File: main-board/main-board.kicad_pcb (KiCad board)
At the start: 2 copper layers, 210 x 130 mm, 172 parts, among them J1 PWR_SELECT, J10 Conn_02x05_Odd_Even, J11 Conn_02x05_Odd_Even, J12 Conn_02x05_Odd_Even, J13 Conn_02x05_Odd_Even, J14 Conn_02x05_Odd_Even, J15 Conn_02x05_Odd_Even, J16 COMM_3, J17 Modular board connector, J18 PWR_EXT_1, J19 PWR_EXT_2, J2 COMM1, J20 COMM_4, J21 COMM_OUT, J3 ICSP, J4 Conn_02x03_Top_Bottom, J5 COMM_2, J7 Conn_02x05_Odd_Even, J8 Conn_02x05_Odd_Even, J9 Conn_02x05_Odd_Even, SW1 RESET, SW10 SW_Push, SW11 SW_Push, SW12 SW_SP3T_x08, SW13 SW_Push, SW14 SW_Push, SW15 SW_Push, SW16 SW_Push, SW17 SW_Push, SW18 SW_Push, SW19 SW_Push, SW2 BTN_LEVEL, SW20 SW_Push, SW21 SW_SP3T_x08, SW22 SW_Push, SW23 SW_Push, SW24 SW_Push, SW25 SW_Push, SW26 SW_Push, SW27 SW_Push, SW28 SW_Push, SW29 SW_Push, SW3 LED_GND, SW30 SW_SP3T_x08, SW31 SW_Push, SW32 SW_Push, SW33 SW_Push, SW34 SW_Push, SW35 SW_Push, SW36 SW_Push, SW37 SW_Push, SW38 SW_Push, SW39 SW_SP3T_x08, SW4 SW_Push, SW41 PWR_EN, SW5 SW_Push, SW6 SW_Push, SW7 SW_Push, SW8 SW_Push, SW9 SW_Push, U1 LM2576HVS-5, U2 AP1117-33, U3 AP1117-18, U4 FT232RL

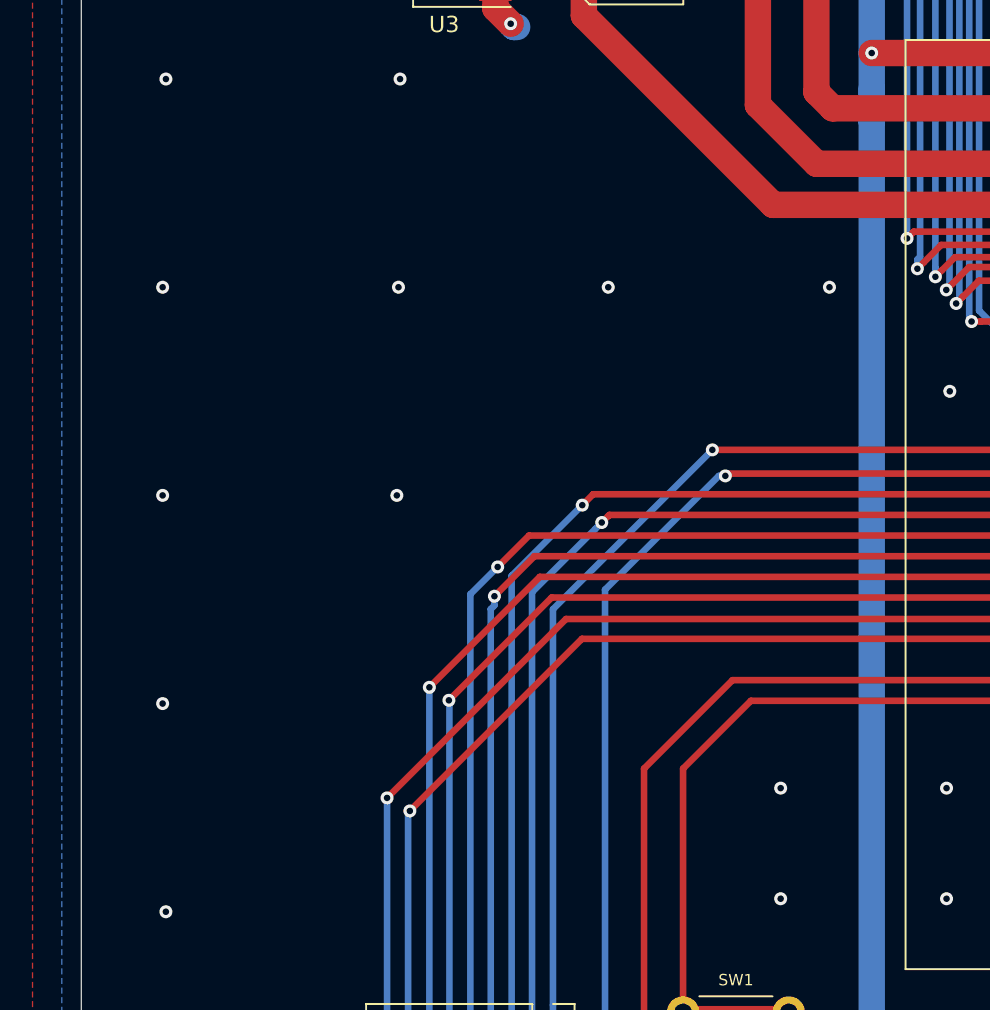
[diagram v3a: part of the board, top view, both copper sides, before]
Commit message: Added module board hole
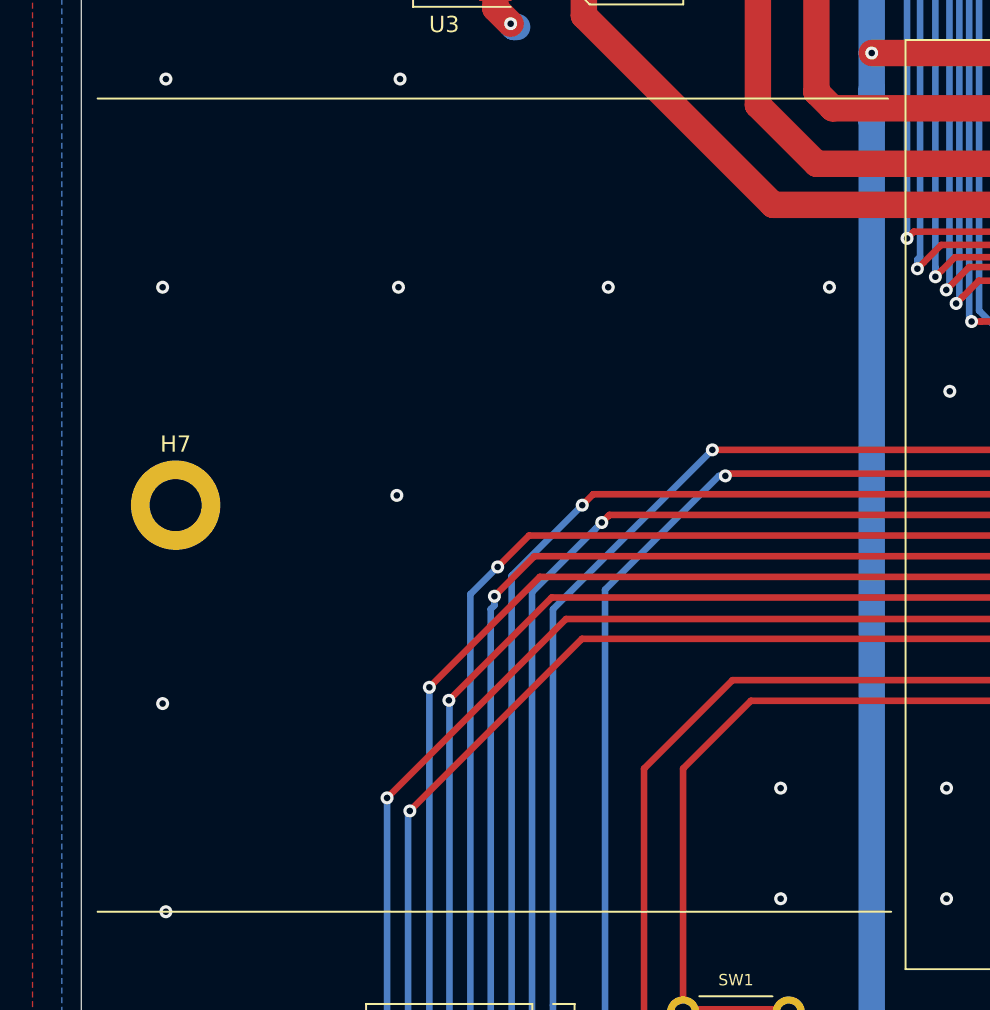
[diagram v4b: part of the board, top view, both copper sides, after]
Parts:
- added H7: MountingHole_Pad, MountingHole:MountingHole_3.2mm_M3_ISO14580_Pad, F.Cu at (42.8, 108.8)
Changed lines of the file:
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@@
   (general
     (thickness 1.6)
-    (drawings 78)
+    (drawings 83)
     (tracks 2027)
     (zones 0)
-    (modules 172)
+    (modules 173)
     (nets 137)
   )
   (page A4)
   (layers
-    (0 F.Cu signal)
-    (31 B.Cu signal)
+    (0 F.Cu signal hide)
+    (31 B.Cu signal hide)
     (32 B.Adhes user hide)
     (33 F.Adhes user hide)
@@
     (38 B.Mask user hide)
     (39 F.Mask user)
-    (40 Dwgs.User user hide)
+    (40 Dwgs.User user)
     (41 Cmts.User user hide)
     (42 Eco1.User user hide)
     (43 Eco2.User user hide)
     (44 Edge.Cuts user)
-    (45 Margin user hide)
+    (45 Margin user)
     (46 B.CrtYd user hide)
     (47 F.CrtYd user hide)
@@
     (add_net "Net-(J17-Pad30)")
     (add_net "Net-(J17-Pad32)")
+    (add_net "Net-(J17-Pad34)")
+    (add_net "Net-(J17-Pad56)")
     (add_net "Net-(J17-Pad58)")
     (add_net "Net-(J17-Pad60)")
+    (add_net "Net-(J17-Pad75)")
     (add_net "Net-(J21-Pad2)")
     (add_net "Net-(J21-Pad3)")
@@
     (add_net "Net-(R7-Pad1)")
     (add_net "Net-(R7-Pad2)")
+    (add_net "Net-(SW41-Pad3)")
+    (add_net "Net-(U4-Pad10)")
+    (add_net "Net-(U4-Pad12)")
+    (add_net "Net-(U4-Pad13)")
+    (add_net "Net-(U4-Pad14)")
     (add_net "Net-(U4-Pad15)")
     (add_net "Net-(U4-Pad16)")
+    (add_net "Net-(U4-Pad19)")
+    (add_net "Net-(U4-Pad27)")
+    (add_net "Net-(U4-Pad28)")
+    (add_net "Net-(U4-Pad4)")
+    (add_net "Net-(U4-Pad6)")
+    (add_net "Net-(U4-Pad9)")
     (add_net VBUS)
   )
@@
     (uvia_drill 0.1)
   )
+  (module MountingHole:MountingHole_3.2mm_M3_ISO14580_Pad (layer F.Cu)
+    (at 42.8 108.8)
+    (descr "Mounting Hole 3.2mm, M3, ISO14580")
+    (tags "mounting hole 3.2mm m3 iso14580")
+    (attr virtual)
+    (fp_text reference H7 (at 0 -3.75) (layer F.SilkS)
+      (effects (font (size 1 1) (thickness 0.15)))
+    )
+    (fp_text value MountingHole_Pad (at 0 3.75) (layer F.Fab)
+      (effects (font (size 1 1) (thickness 0.15)))
+    )
+    (fp_circle (center 0 0) (end 3 0) (layer F.CrtYd) (width 0.05))
+    (fp_circle (center 0 0) (end 2.75 0) (layer Cmts.User) (width 0.15))
+    (fp_text user %R (at 0.3 0) (layer F.Fab)
+      (effects (font (size 1 1) (thickness 0.15)))
+    )
+    (pad 1 thru_hole circle (at 0 0) (size 5.5 5.5) (drill 3.2) (layers *.Cu *.Mask)
+      (net 1 GND))
+  )
   (module Connector_PinHeader_2.54mm:PinHeader_2x03_P2.54mm_Vertical (layer F.Cu)
     (at 154 124.4 270)
@@
     )
   )
+  (dimension 25 (width 0.15) (layer Dwgs.User)
+    (gr_text "25,000 mm" (at 29.9 96.3 270) (layer Dwgs.User)
+      (effects (font (size 1 1) (thickness 0.15)))
+    )
+    (feature1 (pts (xy 38 108.8) (xy 30.613579 108.8)))
+    (feature2 (pts (xy 38 83.8) (xy 30.613579 83.8)))
+    (crossbar (pts (xy 31.2 83.8) (xy 31.2 108.8)))
+    (arrow1a (pts (xy 31.2 108.8) (xy 30.613579 107.673496)))
+    (arrow1b (pts (xy 31.2 108.8) (xy 31.786421 107.673496)))
+    (arrow2a (pts (xy 31.2 83.8) (xy 30.613579 84.926504)))
+    (arrow2b (pts (xy 31.2 83.8) (xy 31.786421 84.926504)))
+  )
+  (dimension 50 (width 0.15) (layer Dwgs.User)
+    (gr_text "50,000 mm" (at 20.9 108.8 270) (layer Dwgs.User)
+      (effects (font (size 1 1) (thickness 0.15)))
+    )
+    (feature1 (pts (xy 38 133.8) (xy 21.613579 133.8)))
+    (feature2 (pts (xy 38 83.8) (xy 21.613579 83.8)))
+    (crossbar (pts (xy 22.2 83.8) (xy 22.2 133.8)))
+    (arrow1a (pts (xy 22.2 133.8) (xy 21.613579 132.673496)))
+    (arrow1b (pts (xy 22.2 133.8) (xy 22.786421 132.673496)))
+    (arrow2a (pts (xy 22.2 83.8) (xy 21.613579 84.926504)))
+    (arrow2b (pts (xy 22.2 83.8) (xy 22.786421 84.926504)))
+  )
+  (gr_line (start 84.4 108.8) (end 47 108.8) (layer Dwgs.User) (width 0.15))
+  (gr_line (start 86.8 133.8) (end 38 133.8) (layer F.SilkS) (width 0.12))
+  (gr_line (start 86.6 83.8) (end 38 83.8) (layer F.SilkS) (width 0.12))
+  (dimension 45 (width 0.12) (layer Dwgs.User)
+    (gr_text "45,000 mm" (at 65.3 121.47) (layer Dwgs.User)
+      (effects (font (size 1 1) (thickness 0.15)))
+    )
+    (feature1 (pts (xy 42.8 107.8) (xy 42.8 120.786421)))
+    (feature2 (pts (xy 87.8 107.8) (xy 87.8 120.786421)))
+    (crossbar (pts (xy 87.8 120.2) (xy 42.8 120.2)))
+    (arrow1a (pts (xy 42.8 120.2) (xy 43.926504 119.613579)))
+    (arrow1b (pts (xy 42.8 120.2) (xy 43.926504 120.786421)))
+    (arrow2a (pts (xy 87.8 120.2) (xy 86.673496 119.613579)))
+    (arrow2b (pts (xy 87.8 120.2) (xy 86.673496 120.786421)))
+  )
   (gr_line (start 95.932 57.52) (end 95.932 56.4) (layer F.SilkS) (width 0.4))
   (gr_line (start 98.472 57.52) (end 98.472 56.4) (layer F.SilkS) (width 0.4))
@@
     (arrow2b (pts (xy 51.2 155.8) (xy 52.326504 155.213579)))
   )
-  (dimension 53 (width 0.15) (layer Dwgs.User)
-    (gr_text "53,000 mm" (at 24.7 107.5 270) (layer Dwgs.User)
-      (effects (font (size 1 1) (thickness 0.15)))
-    )
-    (feature1 (pts (xy 87 134) (xy 25.413579 134)))
-    (feature2 (pts (xy 87 81) (xy 25.413579 81)))
-    (crossbar (pts (xy 26 81) (xy 26 134)))
-    (arrow1a (pts (xy 26 134) (xy 25.413579 132.873496)))
-    (arrow1b (pts (xy 26 134) (xy 26.586421 132.873496)))
-    (arrow2a (pts (xy 26 81) (xy 25.413579 82.126504)))
-    (arrow2b (pts (xy 26 81) (xy 26.586421 82.126504)))
-  )
   (dimension 130 (width 0.15) (layer Dwgs.User)

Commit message: Updates
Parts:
- added [BRD_REF]: LOGO_BRD_REF, qboards_aesthetics:logo_url-10mm, F.Cu at (193.4, 138.6)
- added [BRD_REF]: LOGO_BRD_REF, qboards_aesthetics:logo_url-20mm, F.Cu at (62.0, 108.8)
- moved R8 7.60 mm to (136.0, 124.6)
- moved R9 7.60 mm to (136.0, 126.8)
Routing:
- net GND: track 129.5 -> 115.9 mm
- net Net-(J4-Pad2): track 12.2 -> 18.9 mm
- net VBUS: track 886.8 -> 892.5 mm
- net Net-(J4-Pad1): track 13.5 -> 19.0 mm
- net /PORT_D_BTN_LEVEL: track 162.3 -> 161.2 mm
- net /PORT_C_BTN_LEVEL: track 202.2 -> 203.0 mm

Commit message: Updated footprints
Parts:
- removed [BRD_REF]: LOGO_BRD_REF, qboards_aesthetics:logo_url-10mm
- removed [BRD_REF]: LOGO_BRD_REF, qboards_aesthetics:logo_url-20mm
- C1, C2, C3, C4: footprint Capacitor_SMD:CP_Elec_6.3x5.7 -> Capacitor_SMD:CP_Elec_8x10.5
- D5: footprint Diode_SMD:D_0805_2012Metric_Pad1.15x1.40mm_HandSolder -> Diode_SMD:D_SOD-323_HandSoldering
- L1: footprint Inductor_SMD:L_1812_4532Metric_Pad1.30x3.40mm_HandSolder -> Inductor_SMD:L_6.3x6.3_H3
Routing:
- net Net-(C2-Pad1): track 39.6 -> 41.4 mm
- net Net-(J1-Pad3): track 19.6 -> 20.3 mm

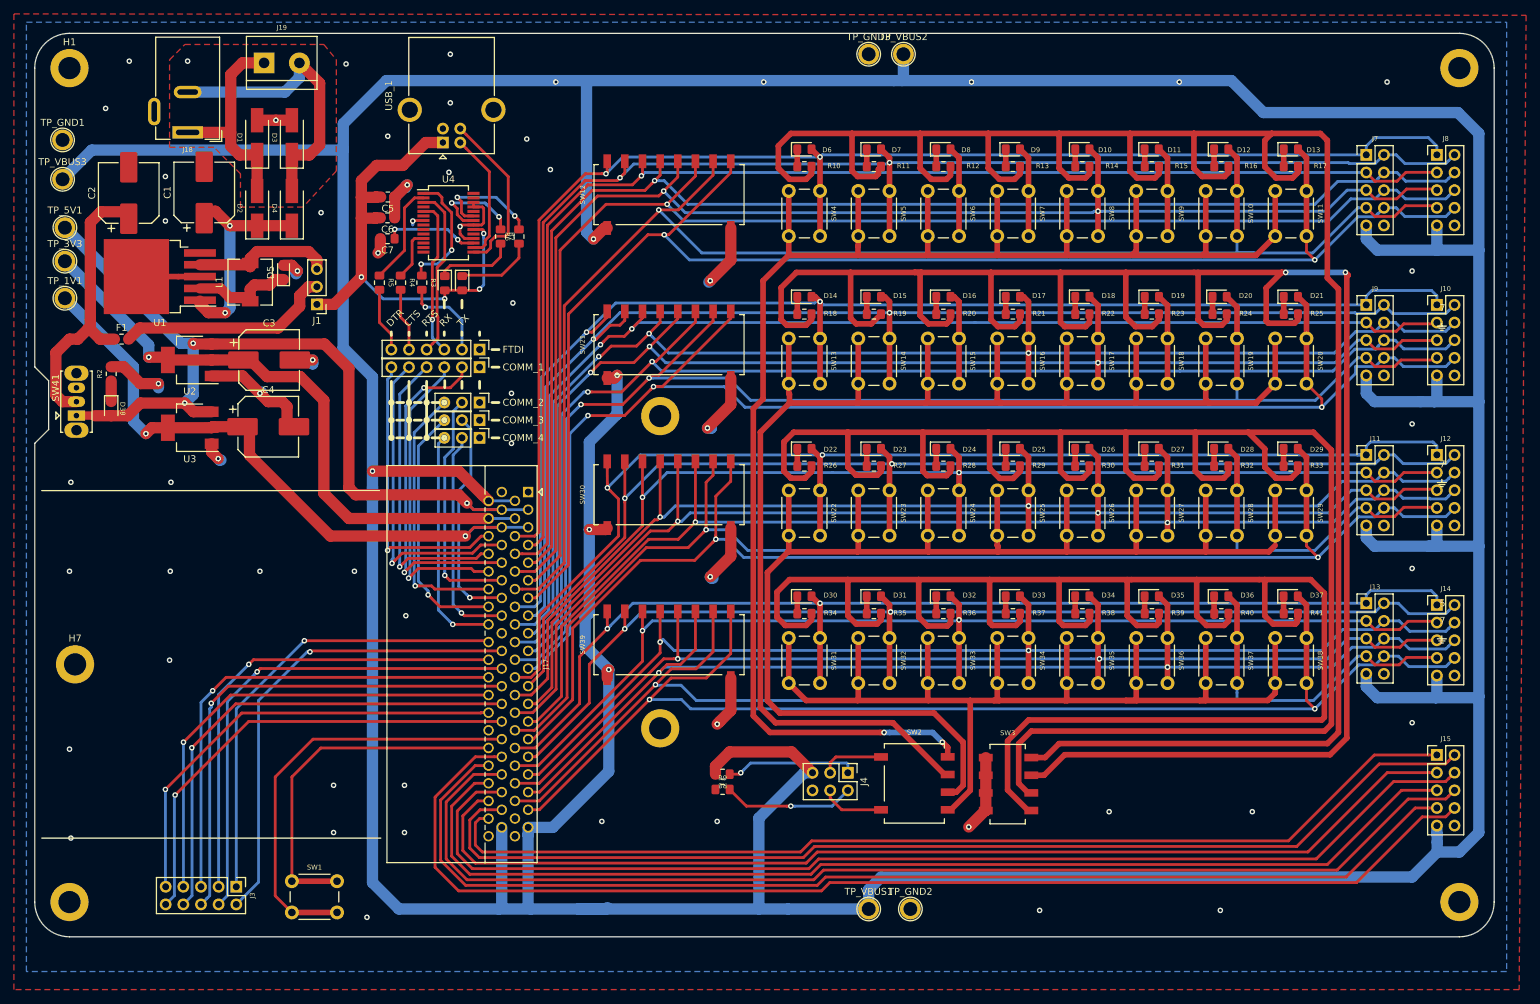
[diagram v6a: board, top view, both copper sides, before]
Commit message: Updated silkscreens
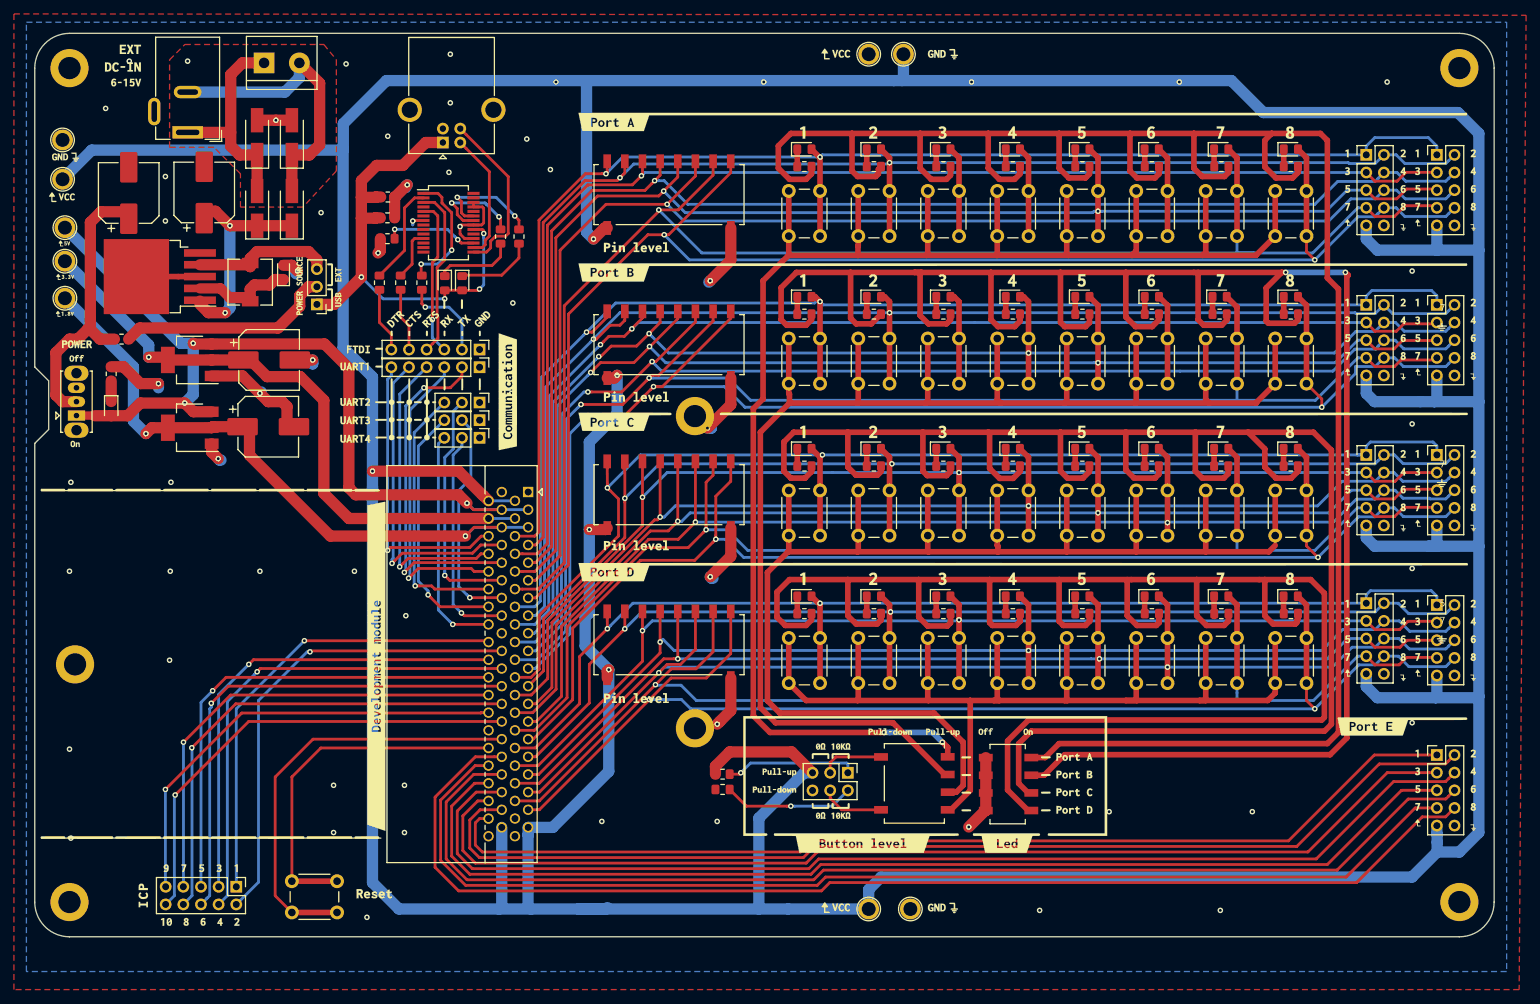
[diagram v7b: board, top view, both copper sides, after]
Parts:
- added ?: , , F.Cu at (90.9, 71.1)
- moved H5 5.00 mm to (132.0, 73.1)
- moved H6 5.00 mm to (132.0, 118.0)
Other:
- board text added: "0\U+03A9"
- board text added: "1"
- board text added: "1.8V"
- board text added: "10"
- board text added: "10K\U+03A9"
- board text added: "2"
- board text added: "3"
- board text added: "3.3V"
- board text added: "4"
- board text added: "5V"
- board text added: "6"
- board text added: "6-15V"
- board text added: "8"
- board text added: "9"
- board text added: "Button level"
- board text added: "Communication"
- board text added: "DC-IN"
- board text added: "Development module"
- board text added: "EXT"
- board text added: "GND"
- board text added: "ICP"
- board text added: "Led"
- board text added: "Off"
- board text added: "On"
- board text added: "POWER"
- board text added: "POWER SOURCE"
- board text added: "Pin level"
- board text added: "Port A"
- board text added: "Port B"
- board text added: "Port C"
- board text added: "Port D"
- board text added: "Port E"
- board text added: "Pull-down"
- board text added: "Pull-up"
- board text added: "Reset"
- board text added: "UART1"
- board text added: "UART2"
- board text added: "UART3"
- board text added: "UART4"
- board text added: "USB"
- board text added: "VCC"
- board text removed: "COMM_1"
- board text removed: "COMM_2"
- board text removed: "COMM_3"
- board text removed: "COMM_4"

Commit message: Cleaned up Dwgs.User
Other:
- board text removed: "0\U+03A9"
- board text removed: "1"
- board text removed: "1.8V"
- board text removed: "10"
- board text removed: "10K\U+03A9"
- board text removed: "2"
- board text removed: "3"
- board text removed: "3.3V"
- board text removed: "4"
- board text removed: "5V"
- board text removed: "6"
- board text removed: "6-15V"
- board text removed: "8"
- board text removed: "9"
- board text removed: "Button level"
- board text removed: "CTS"
- board text removed: "Communication"
- board text removed: "DC-IN"
- board text removed: "DTR"
- board text removed: "Development module"
- board text removed: "EXT"
- board text removed: "FTDI"
- board text removed: "GND"
- board text removed: "ICP"
- board text removed: "Led"
- board text removed: "Off"
- board text removed: "On"
- board text removed: "POWER"
- board text removed: "POWER SOURCE"
- board text removed: "Pin level"
- board text removed: "Port A"
- board text removed: "Port B"
- board text removed: "Port C"
- board text removed: "Port D"
- board text removed: "Port E"
- board text removed: "Pull-down"
- board text removed: "Pull-up"
- board text removed: "RTS"
- board text removed: "RX"
- board text removed: "Reset"
- board text removed: "TX"
- board text removed: "UART1"
- board text removed: "UART2"
- board text removed: "UART3"
- board text removed: "UART4"
- board text removed: "USB"
- board text removed: "VCC"
